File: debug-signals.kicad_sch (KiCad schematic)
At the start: 77 parts, among them U12 TCA9534PWR, U13 TCA9534PWR, U14 Si7021, U15 TCA9534PWR, U16 TCA9534PWR

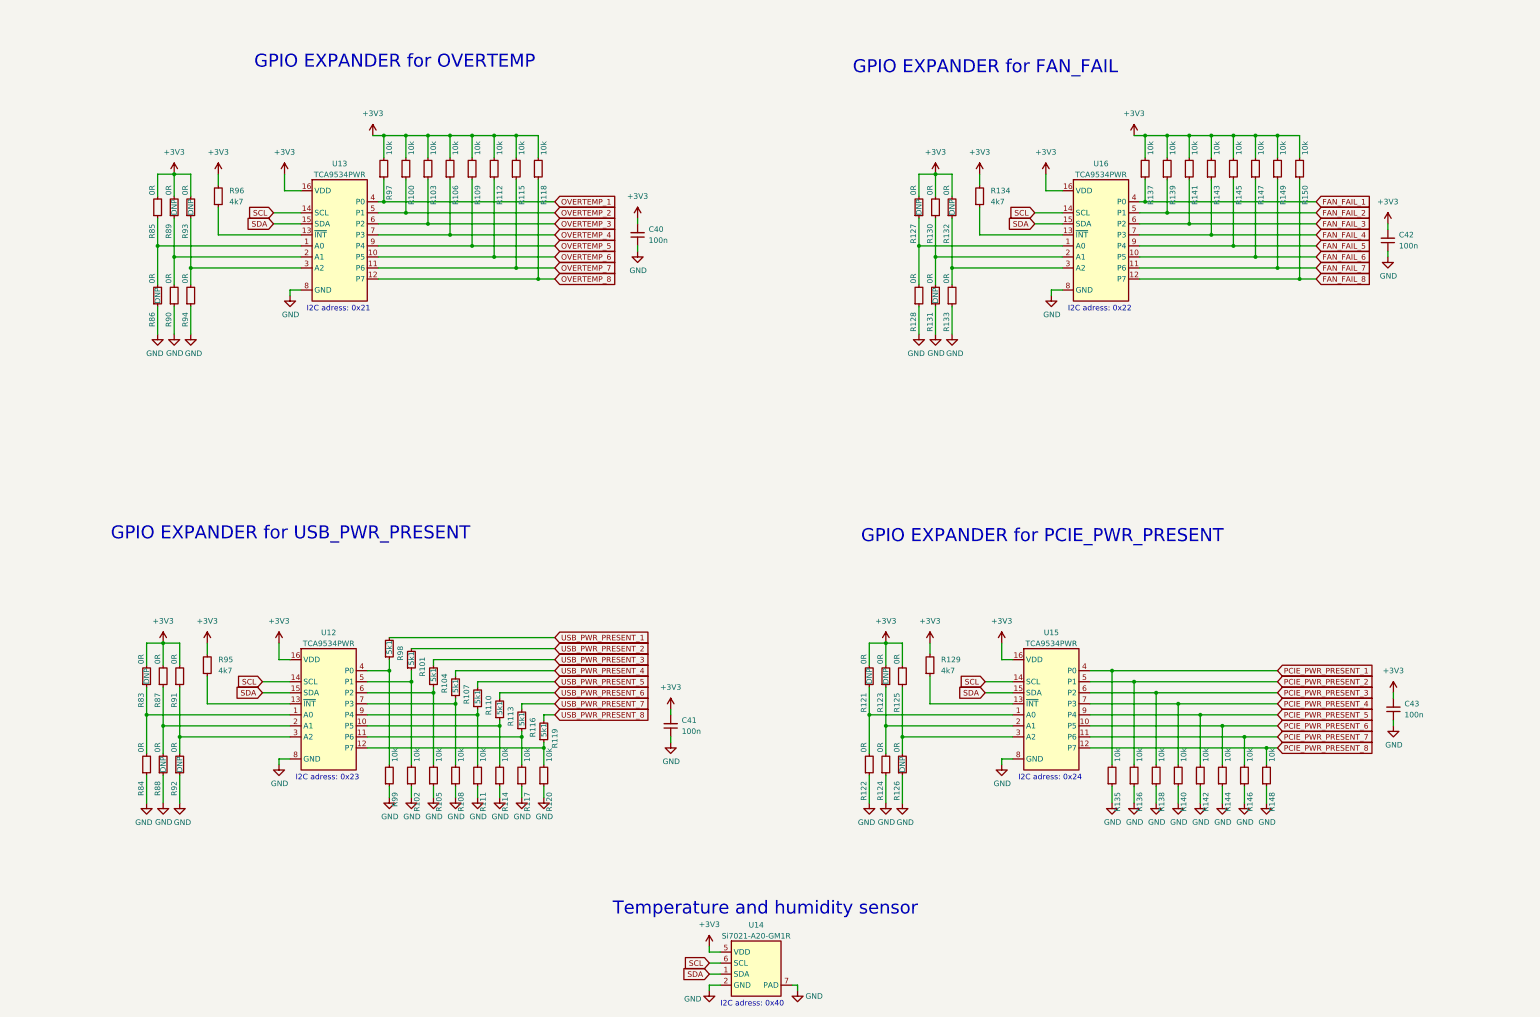
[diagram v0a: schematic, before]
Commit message: Placement of supply section on PCB
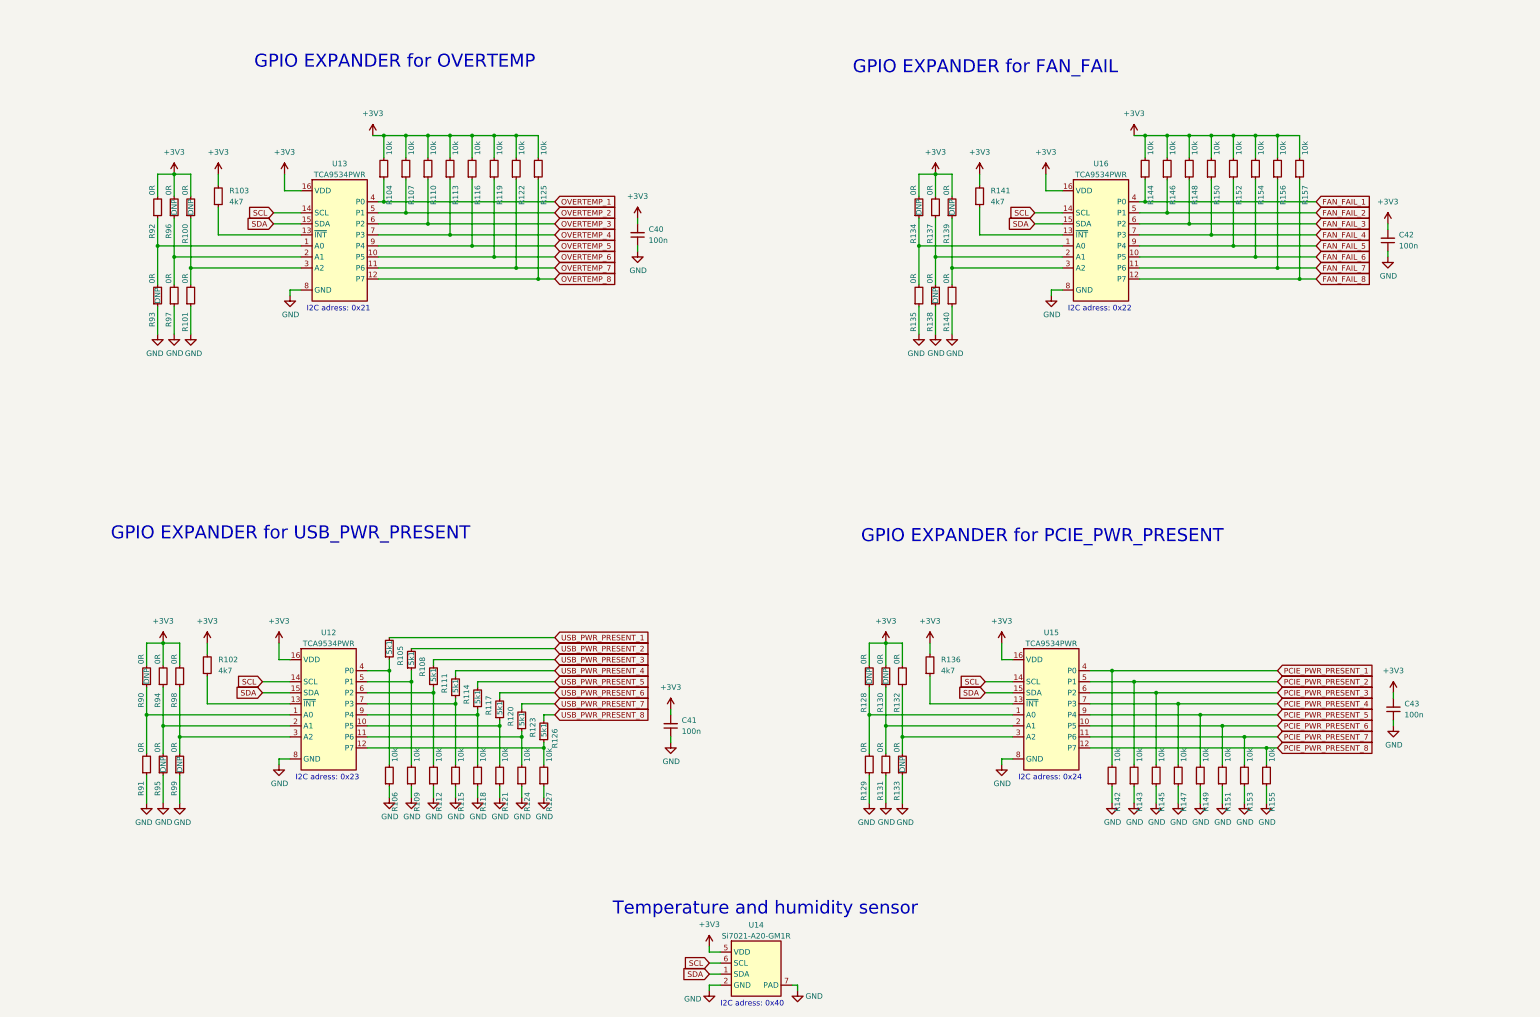
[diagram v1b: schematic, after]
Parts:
- renumbered R93 to R100, R94 to R101, R95 to R102, R96 to R103, R97 to R104, R98 to R105, R99 to R106, R100 to R107, R101 to R108, R102 to R109, R103 to R110, R104 to R111, R105 to R112, R106 to R113, R107 to R114, R108 to R115, R109 to R116, R110 to R117, R111 to R118, R112 to R119, R113 to R120, R114 to R121, R115 to R122, R116 to R123, R117 to R124, R118 to R125, R119 to R126, R120 to R127, R121 to R128, R122 to R129, R123 to R130, R124 to R131, R125 to R132, R126 to R133, R127 to R134, R128 to R135, R129 to R136, R130 to R137, R131 to R138, R132 to R139, R133 to R140, R134 to R141, R135 to R142, R136 to R143, R137 to R144, R138 to R145, R139 to R146, R140 to R147, R141 to R148, R142 to R149, R143 to R150, R144 to R151, R145 to R152, R146 to R153, R147 to R154, R148 to R155, R149 to R156, R150 to R157, R83 to R90, R84 to R91, R85 to R92, R86 to R93, R87 to R94, R88 to R95, R89 to R96, R90 to R97, R91 to R98, R92 to R99

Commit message: Implement changes suggested in schematic review
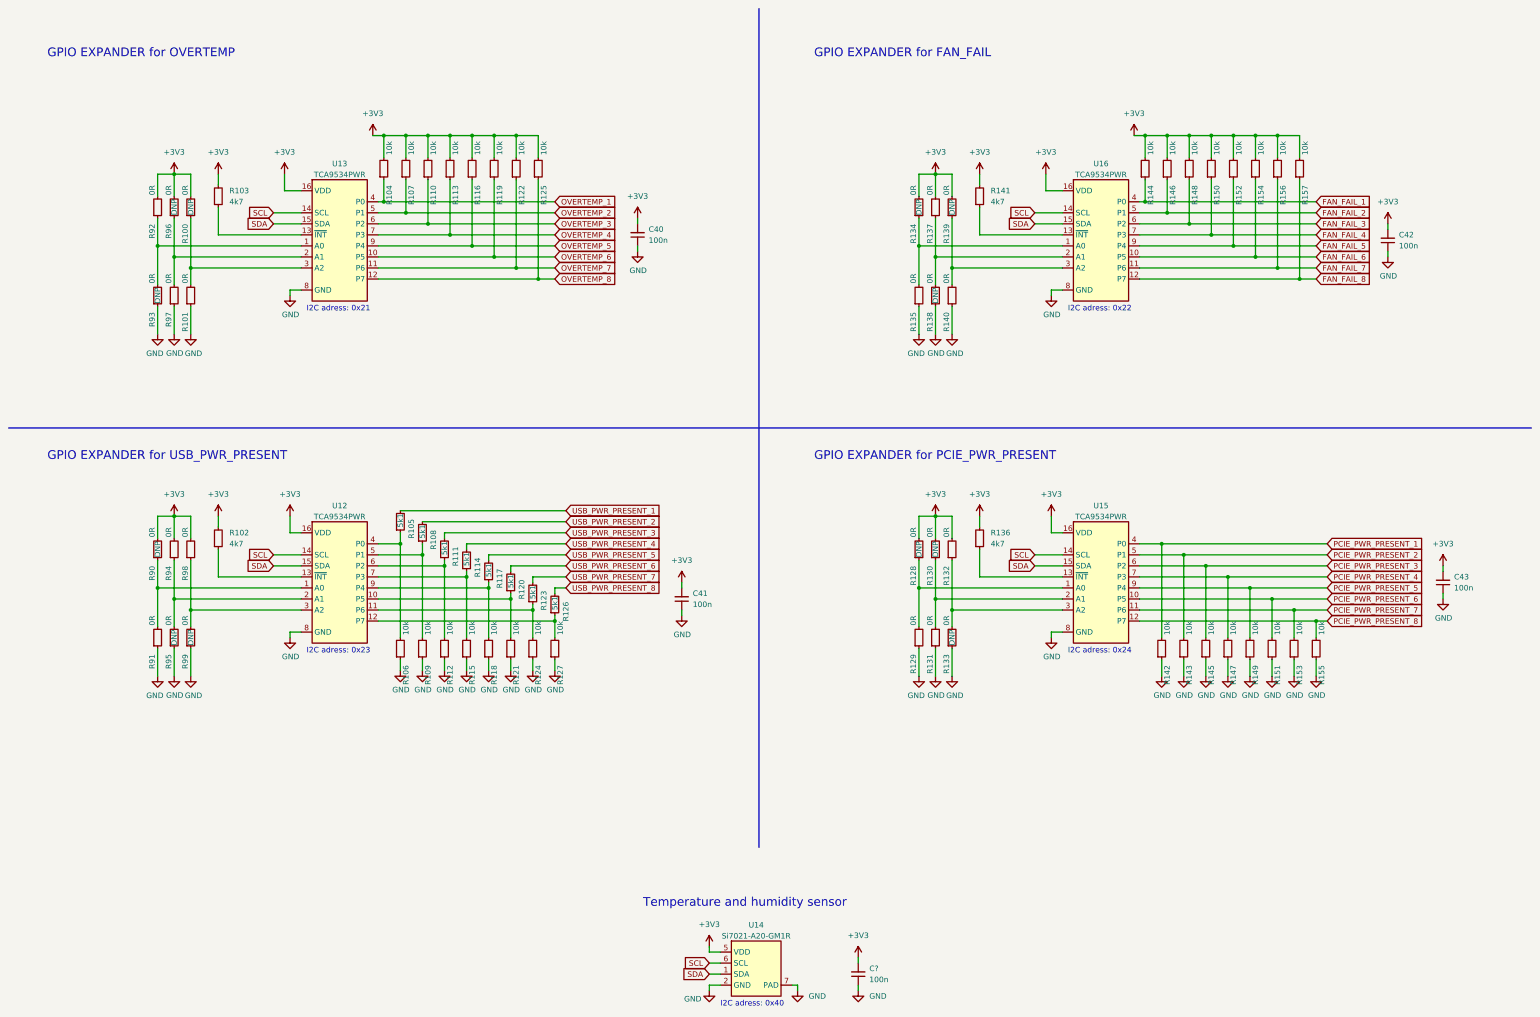
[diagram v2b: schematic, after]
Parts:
- added C?: C_100n_0402, antmicro-footprints:C_0402_1005Metric, symbol antmicroCapacitors0402:C_100n_0402
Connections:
- net +3V3: now also C?.2
- net GND: now also C?.1
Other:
- company: (none) -> Antmicro Ltd
- moved on the sheet: C41, C43, R102, R105, R106, R108, R109, R111, R112, R114, R115, R117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

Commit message: 2nd part of review changes
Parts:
- gave numbers to parts that had none: 1

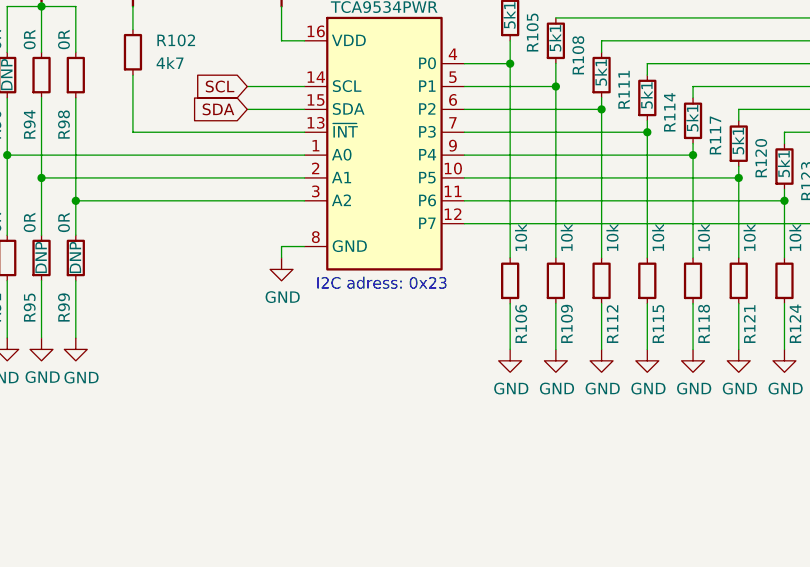
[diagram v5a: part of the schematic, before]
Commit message: Fix adress on schematic
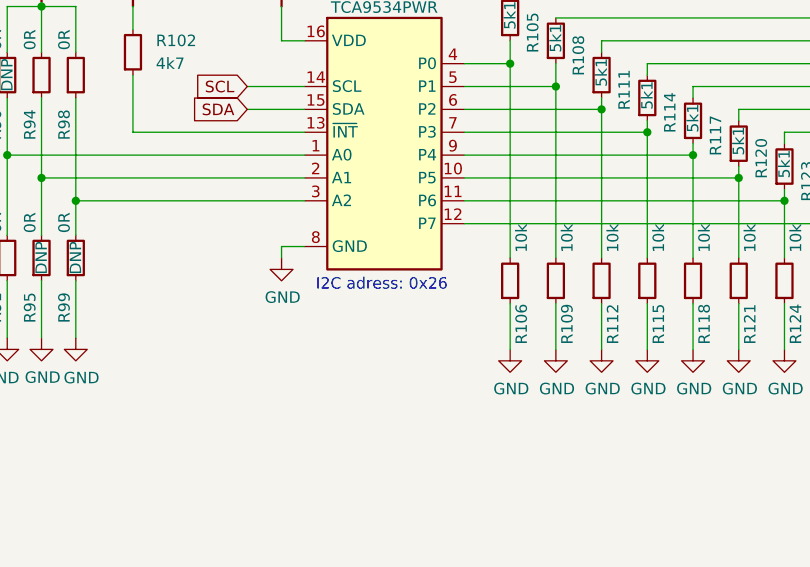
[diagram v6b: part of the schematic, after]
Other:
- note added: "I2C adress: 0x26"
- note removed: "I2C adress: 0x23"
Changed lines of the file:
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@@
     (effects (font (size 1.27 1.27)) (justify left bottom))
   )
-  (text "I2C adress: 0x23\n" (at 105.41 172.72 0)
+  (text "I2C adress: 0x26\n" (at 105.41 172.72 0)
     (effects (font (size 1.27 1.27)) (justify left bottom))
   )

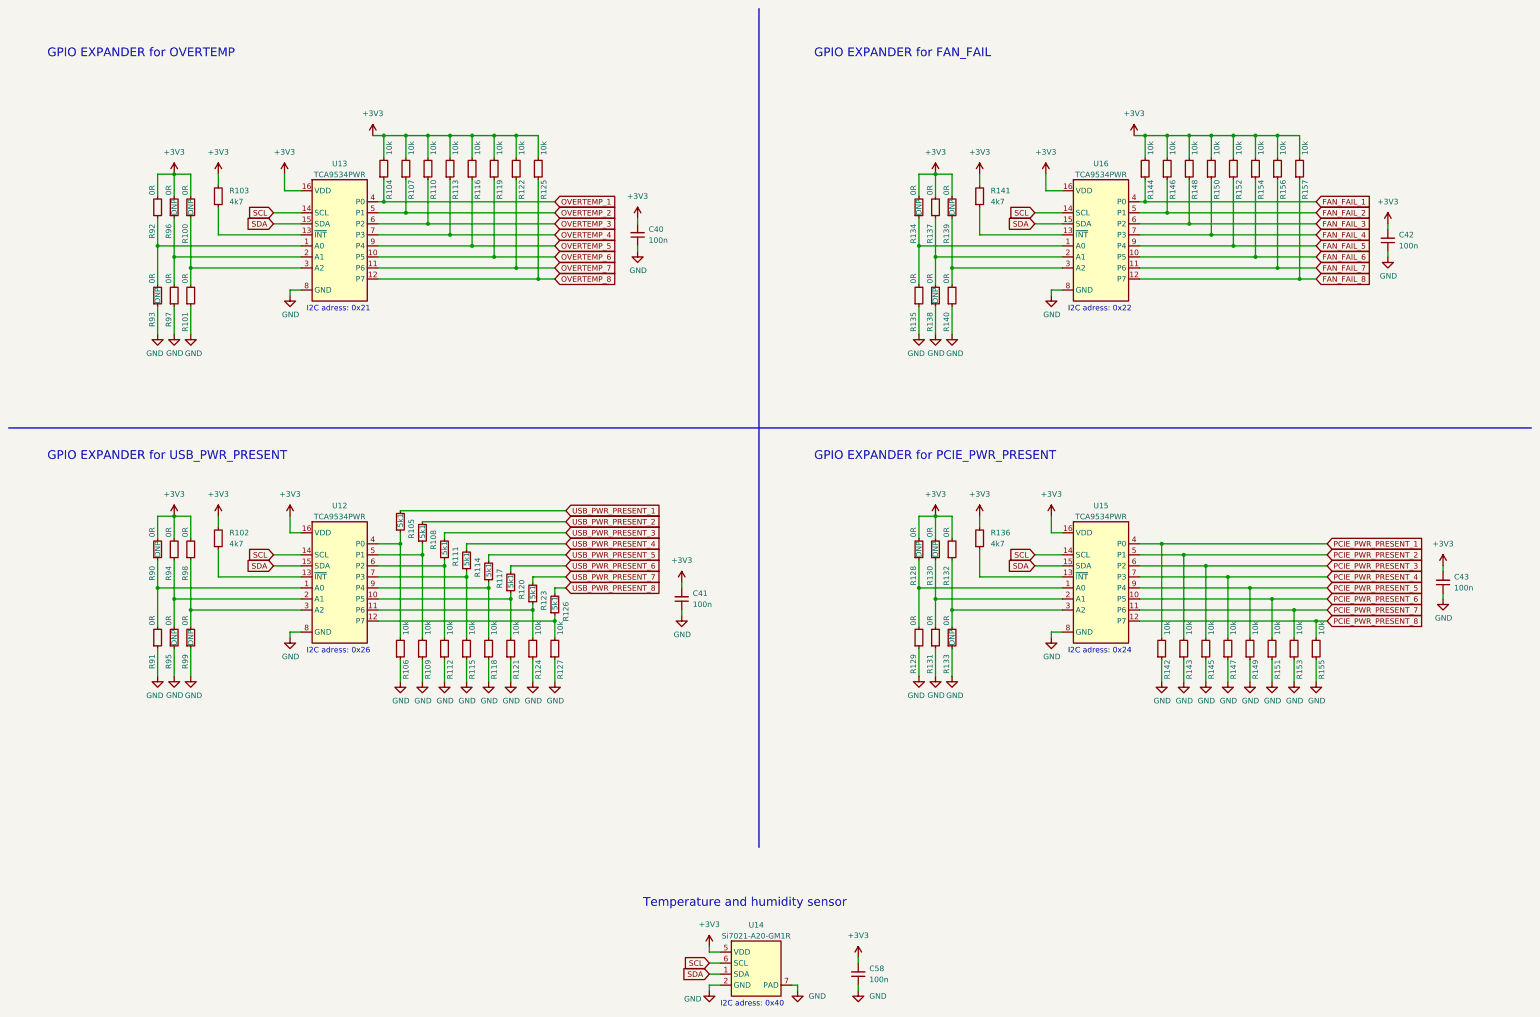
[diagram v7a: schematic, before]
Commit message: Replace symbols with alternatives from main component library
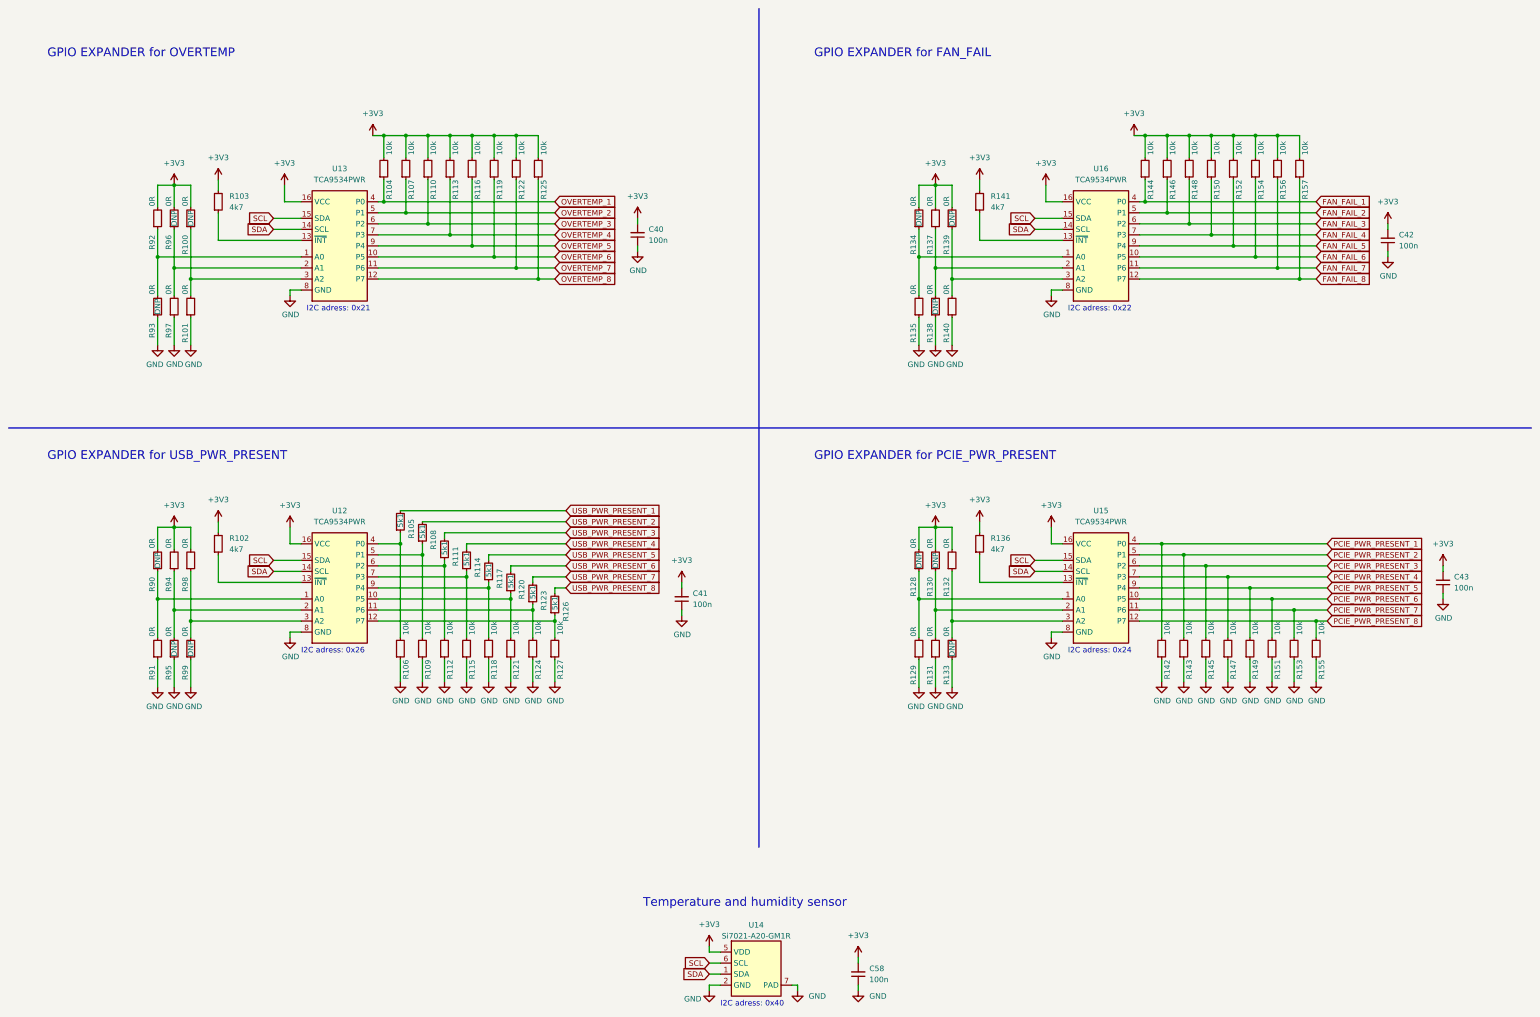
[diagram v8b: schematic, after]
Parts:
- removed U12, U13, U15, U16: TCA9534PWR, antmicro-footprints:TSSOP-16_4.4x5mm_P0.65mm, symbol antmicroInterfaceIOExpanders:TCA9534PWR
- added U12, U13, U15, U16: TCA9534PWR_TSSOP, antmicro-footprints:TSSOP-16_4.4x5mm_P0.65mm, symbol antmicroInterfaceIOExpanders:TCA9534PWR_TSSOP
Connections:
- net +3V3: now also U12.16 (VCC), U13.16 (VCC), U15.16 (VCC), U16.16 (VCC)
- net FAN_FAIL_1: now also U16.4 (P0)
- net FAN_FAIL_2: now also U16.5 (P1)
- net FAN_FAIL_3: now also U16.6 (P2)
- net FAN_FAIL_4: now also U16.7 (P3)
- net FAN_FAIL_5: now also U16.9 (P4)
- net FAN_FAIL_6: now also U16.10 (P5)
- net FAN_FAIL_7: now also U16.11 (P6)
- net FAN_FAIL_8: now also U16.12 (P7)
- net GND: now also U12.8 (GND), U13.8 (GND), U15.8 (GND), U16.8 (GND)
- net OVERTEMP_1: now also U13.4 (P0)
- net OVERTEMP_2: now also U13.5 (P1)
- net OVERTEMP_3: now also U13.6 (P2)
- net OVERTEMP_4: now also U13.7 (P3)
- net OVERTEMP_5: now also U13.9 (P4)
- net OVERTEMP_6: now also U13.10 (P5)
- net OVERTEMP_7: now also U13.11 (P6)
- net OVERTEMP_8: now also U13.12 (P7)
- net PCIE_PWR_PRESENT_1: now also U15.4 (P0)
- net PCIE_PWR_PRESENT_2: now also U15.5 (P1)
- net PCIE_PWR_PRESENT_3: now also U15.6 (P2)
- net PCIE_PWR_PRESENT_4: now also U15.7 (P3)
- net PCIE_PWR_PRESENT_5: now also U15.9 (P4)
- net PCIE_PWR_PRESENT_6: now also U15.10 (P5)
- net PCIE_PWR_PRESENT_7: now also U15.11 (P6)
- net PCIE_PWR_PRESENT_8: now also U15.12 (P7)
- net SCL: now also U12.15 (SDA), U13.15 (SDA), U15.15 (SDA), U16.15 (SDA)
- net SDA: now also U12.14 (SCL), U13.14 (SCL), U15.14 (SCL), U16.14 (SCL)
- net at R100.1, R101.2: now also U13.3 (A2)
- net at R96.1, R97.2: now also U13.2 (A1)
- net at R132.1, R133.2: now also U15.3 (A2)
- net at R117.1, R118.2: now also U12.9 (P4)
- net at R90.1, R91.2: now also U12.1 (A0)
- net at R120.1, R121.2: now also U12.10 (P5)
- net at R123.1, R124.2: now also U12.11 (P6)
- net at R126.1, R127.2: now also U12.12 (P7)
- net at R102.1: now also U12.13 (~{INT})
- net at R94.1, R95.2: now also U12.2 (A1)
- net at R98.1, R99.2: now also U12.3 (A2)
- net at R105.1, R106.2: now also U12.4 (P0)
- net at R108.1, R109.2: now also U12.5 (P1)
- net at R111.1, R112.2: now also U12.6 (P2)
- net at R114.1, R115.2: now also U12.7 (P3)
- net at R134.1, R135.2: now also U16.1 (A0)
- net at R141.1: now also U16.13 (~{INT})
- net at R137.1, R138.2: now also U16.2 (A1)
- net at R139.1, R140.2: now also U16.3 (A2)
- net at R92.1, R93.2: now also U13.1 (A0)
- net at R103.1: now also U13.13 (~{INT})
- net at R128.1, R129.2: now also U15.1 (A0)
- net at R130.1, R131.2: now also U15.2 (A1)
- net at R136.1: now also U15.13 (~{INT})
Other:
- moved on the sheet: R100, R101, R102, R103, R128, R129, R130, R131, R132, R133, R134, R135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
